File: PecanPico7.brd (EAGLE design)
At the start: 34.2 x 50 mm, 177 parts, among them IC1 Si4464-B1B-FM, IC10 TC1185-1.8VCT713, IC11 TC1185-2.5VCT713, IC12 ADR380ARTZ, IC13 RF6886, IC15 MPU-9250, IC16 PAC1720-1-AIA-TR, IC2 Si4464-B1B-FM, IC3 BME280_BME280, IC4 UBLOX_MAX-6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

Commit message: Fixed incorrect voltage supply at OV2640
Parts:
- removed C55: 470pF, PecanPico6:0402
- removed C56, C57: 1uF, PecanPico6:0402
- removed C58: 100nF, PecanPico6:0402
- removed IC11: TC1185-2.5VCT713, stm32f42x:SOT95P290X145-5N
- removed IC12: ADR380ARTZ, stm32f4:SOT95P237X112-3N
- IC10: value TC1185-1.8VCT713 -> LP5951MF-1.3/NOPB
- TCXO: value TXC_7Z -> TG-5006CJ-19H
- moved R39 17.0 mm to (22.7, 12.8), turned to 270 degrees
- moved R40 15.5 mm to (21.6, 12.8), turned to 270 degrees
- moved C34 6.08 mm to (26.4, 18.3), flipped to the top
- moved C40 4.24 mm to (14.6, 10.8), turned to 270 degrees
- moved R22 3.62 mm to (23.0, 11.4), turned to 0 degrees
- moved R25 3.60 mm to (15.0, 8.20), turned to 90 degrees
- moved C54 2.88 mm to (18.2, 8.80), turned to 0 degrees
- moved Q2 2.75 mm to (20.2, 10.4), turned to 90 degrees
- moved R32 2.51 mm to (30.0, 13.7), turned to 90 degrees
- moved IC10 2.14 mm to (16.8, 11.5)
- moved C30 2.02 mm to (21.0, 21.1)
- moved C42 1.75 mm to (16.4, 7.70), turned to 180 degrees
- moved C41 1.49 mm to (16.4, 8.80)
- moved C53 1.39 mm to (19.0, 13.2), turned to 270 degrees
- moved R31 1.20 mm to (28.9, 13.7), turned to 90 degrees
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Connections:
- net CAM_VCC1V8 renamed CAM_VCC1V3
- removed net CAM_VCC3V0: C43.P$1, C53.P$2, C56.P$2, IC10.1, IC10.3, IC11.1, IC11.3, Q2.3, X1.11, X1.6
- removed net N$28: C55.P$2, IC11.4
- removed net N$30: C37.P$1, C39.P$1, IC12.2, IC5.P1
- net CAM_VCC2V5: now also C43.P$1, C53.P$2, IC10.1, IC10.3, Q2.3, R39.P$2, R40.P$2, X1.11, X1.6; no longer C57.P$2, IC11.5
- net GND: no longer C55.P$1, C56.P$1, C57.P$1, C58.P$2, IC11.2, IC12.3
- net VCC: now also C37.P$1, C39.P$1, IC5.P1; no longer C58.P$1, IC12.1, R39.P$2, R40.P$2
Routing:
- net CAM_VCC3V0: track 25.3 -> 0.00 mm
- net CAM_VCC2V5: track 5.85 -> 24.8 mm
- net CAM_SIOC: track 27.4 -> 16.5 mm, vias 3 -> 2
- net CAM_SIOD: track 28.8 -> 18.2 mm, vias 3 -> 2
- net LED2: track 31.6 -> 25.3 mm, vias 3 -> 1
- net AGND: track 8.84 -> 3.30 mm, vias 2 -> 0
- net VCC: track 284.5 -> 279.1 mm, vias 26 -> 25
- net CAM_OFF: track 4.94 -> 10.1 mm
- net N$30: track 4.54 -> 0.00 mm
- net NRST: track 25.1 -> 21.7 mm
- net GND: track 16.1 -> 18.2 mm, vias 168 -> 178
- net N$48: track 0.98 -> 3.02 mm
- net LED1: track 22.5 -> 20.6 mm
- net N$28: track 1.31 -> 0.00 mm
- net SD_MISO: track 14.2 -> 13.3 mm
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
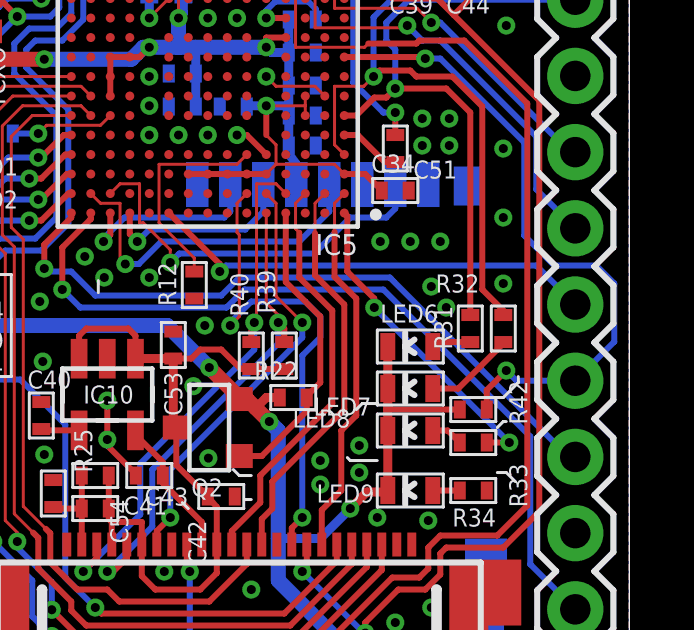
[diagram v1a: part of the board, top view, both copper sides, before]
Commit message: Moved parts around
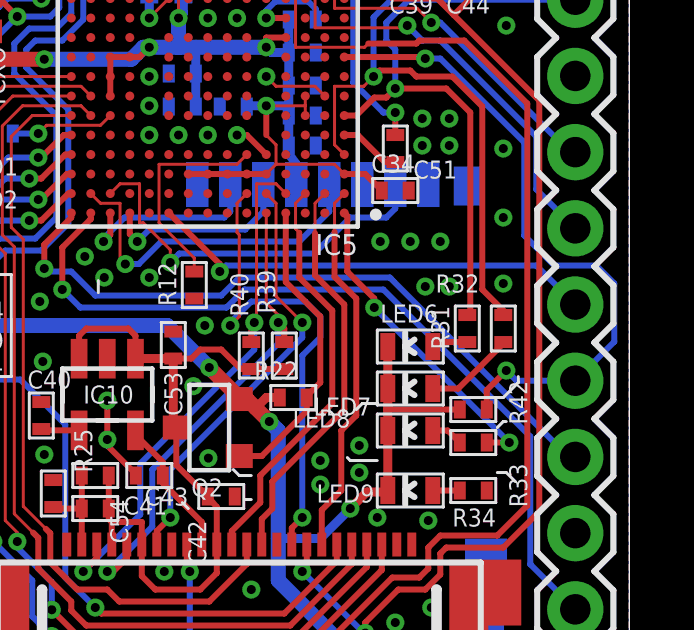
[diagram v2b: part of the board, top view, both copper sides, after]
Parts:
- moved R31 0.10 mm to (28.8, 13.7)
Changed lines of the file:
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@@
 <attribute name="VALUE" x="28" y="9.7" size="0.6" layer="27" rot="R180"/>
 </element>
-<element name="R31" library="PecanPico6" package="0402" value="3.3k" x="28.9" y="13.7" smashed="yes" rot="R90">
-<attribute name="NAME" x="28.3" y="13" size="0.6" layer="25" rot="R90"/>
-<attribute name="VALUE" x="30.1" y="13" size="0.6" layer="27" rot="R90"/>
+<element name="R31" library="PecanPico6" package="0402" value="3.3k" x="28.8" y="13.7" smashed="yes" rot="R90">
+<attribute name="NAME" x="28.2" y="13" size="0.6" layer="25" rot="R90"/>
+<attribute name="VALUE" x="30" y="13" size="0.6" layer="27" rot="R90"/>
 </element>
 <element name="R32" library="PecanPico6" package="0402" value="1k" x="30" y="13.7" smashed="yes" rot="R90">
@@
 <via x="12.63" y="32.5" extent="1-16" drill="0.3"/>
 <via x="27.9" y="16.6" extent="1-16" drill="0.3"/>
-<via x="28.1" y="14.4" extent="1-16" drill="0.3"/>
+<via x="28.2" y="15.1" extent="1-16" drill="0.3"/>
 <via x="16.4" y="49" extent="1-16" drill="0.3"/>
 <via x="24.3" y="42.9" extent="1-16" drill="0.3"/>
@@
 <contactref element="X1" pad="P$3"/>
 <contactref element="X1" pad="P$4"/>
-<via x="27.6" y="15.1" extent="1-16" drill="0.3"/>
+<via x="27.4" y="15.1" extent="1-16" drill="0.3"/>
 <via x="16.8" y="11.3" extent="1-16" drill="0.3"/>
 <wire x1="17.75" y1="8.8" x2="17.75" y2="8.85" width="0.2" layer="1"/>
@@
 <contactref element="LED6" pad="A"/>
 <contactref element="R31" pad="P$1"/>
-<wire x1="28.9" y1="13.25" x2="27.65" y2="13.25" width="0.2" layer="1"/>
+<wire x1="28.8" y1="13.25" x2="27.65" y2="13.25" width="0.2" layer="1"/>
 <wire x1="27.65" y1="13.25" x2="27.65" y2="13.1" width="0.2" layer="1"/>
 </signal>
@@
 <wire x1="26.4" y1="23" x2="26.1" y2="23.3" width="0.2" layer="16"/>
 <wire x1="26.1" y1="23.3" x2="26.1" y2="23.9" width="0.2" layer="16"/>
-<wire x1="28.9" y1="20.9" x2="28.9" y2="14.15" width="0.2" layer="1"/>
 <wire x1="25.1" y1="20.8" x2="25.7" y2="21.4" width="0.2" layer="1"/>
 <wire x1="25.7" y1="21.4" x2="26.1" y2="21.4" width="0.2" layer="1"/>
@@
 <wire x1="26.1" y1="23.9" x2="26.86" y2="24.66" width="0.2" layer="16"/>
 <wire x1="26.86" y1="24.66" x2="32.4" y2="24.66" width="0.2" layer="16"/>
+<wire x1="28.9" y1="20.9" x2="28.9" y2="14.15" width="0.2" layer="1"/>
+<wire x1="28.9" y1="14.15" x2="28.8" y2="14.15" width="0.2" layer="1"/>
 </signal>
 <signal name="LED3">

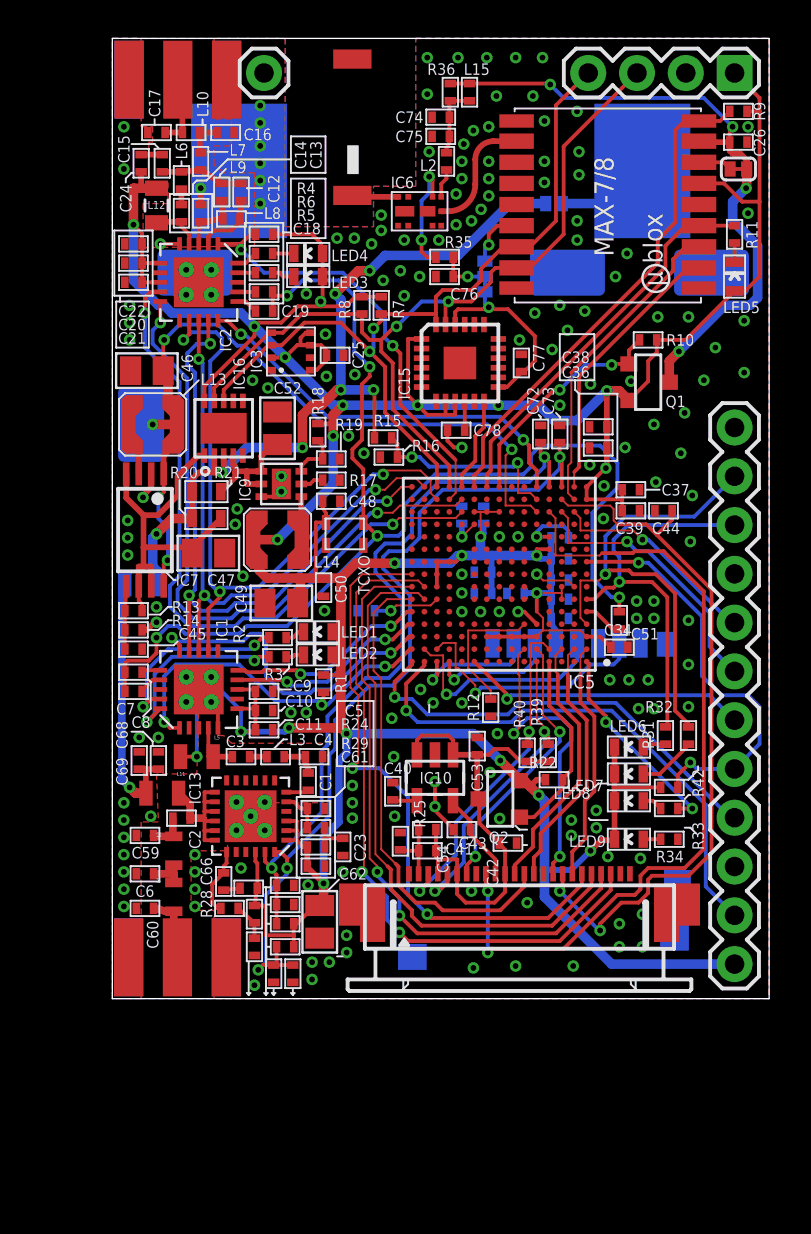
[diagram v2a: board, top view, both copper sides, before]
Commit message: Relocated names, added infos, added PCB name
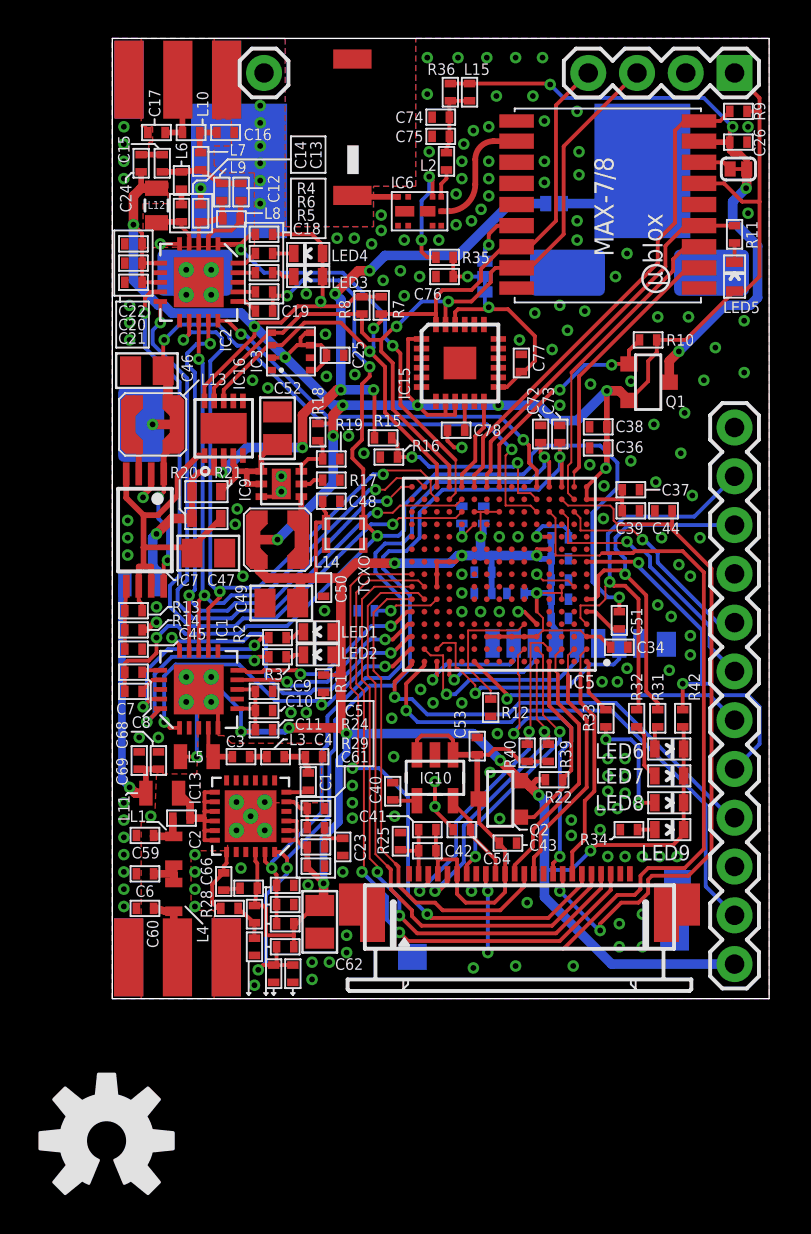
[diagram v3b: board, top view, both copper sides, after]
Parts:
- added LOGO1: OSHW-LOGOL, PecanPico6:OSHW-LOGO-L
- IC10: value LP5951MF-1.3/NOPB -> (none)
- moved R33 5.74 mm to (25.7, 14.6), turned to 90 degrees
- moved R42 3.67 mm to (29.7, 14.6), turned to 270 degrees
- moved R32 2.85 mm to (27.3, 14.6)
- moved LED9 2.16 mm to (29.0, 8.80), turned to 270 degrees
- moved R34 2.16 mm to (26.9, 8.80), turned to 180 degrees
- moved LED8 2.10 mm to (29.0, 10.2), turned to 270 degrees
- moved LED6 2.10 mm to (29.0, 13.0), turned to 270 degrees
- moved LED7 2.10 mm to (29.0, 11.6), turned to 270 degrees
- moved R31 0.98 mm to (28.4, 14.6)
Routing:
- net LED3: track 10.7 -> 2.91 mm, vias 2 -> 0
- net N$49: track 1.07 -> 6.27 mm, vias 0 -> 2
- net LED2: track 25.3 -> 21.6 mm
- net VCC: track 279.1 -> 281.0 mm
- net NRST: track 21.7 -> 20.0 mm
- net LED1: track 20.7 -> 19.6 mm
- net CAM_HREF: track 42.5 -> 43.1 mm
- net GND: vias 178 -> 189
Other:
- board text added: "Dec 2015"
- board text added: "GPSBIAS"
- board text added: "Pecan Pico 7 rev1.0"
- board text removed: "GPS BIAS"

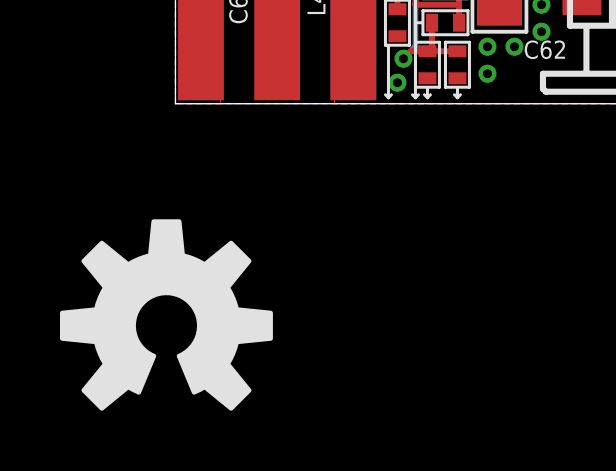
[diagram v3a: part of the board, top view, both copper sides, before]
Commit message: Adjusted symbols
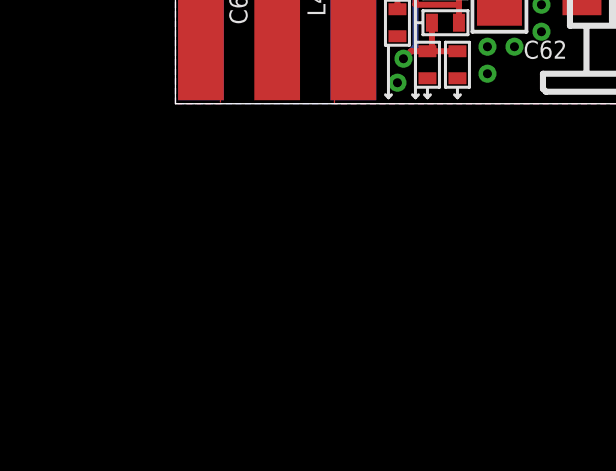
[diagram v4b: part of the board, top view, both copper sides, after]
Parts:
- removed LOGO1: OSHW-LOGOL, PecanPico6:OSHW-LOGO-L
- added LOGO2: OSHW-LOGOM, PecanPico6:OSHW-LOGO-M
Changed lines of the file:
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@@
 <grid distance="0.1" unitdist="mm" unit="mm" style="lines" multiple="1" display="yes" altdistance="0.025" altunitdist="inch" altunit="inch"/>
 <layers>
-<layer number="1" name="Top" color="4" fill="1" visible="yes" active="yes"/>
-<layer number="16" name="Bottom" color="1" fill="1" visible="no" active="yes"/>
+<layer number="1" name="Top" color="4" fill="1" visible="no" active="yes"/>
+<layer number="16" name="Bottom" color="1" fill="1" visible="yes" active="yes"/>
 <layer number="17" name="Pads" color="2" fill="1" visible="yes" active="yes"/>
 <layer number="18" name="Vias" color="2" fill="1" visible="yes" active="yes"/>
 <layer number="19" name="Unrouted" color="6" fill="1" visible="yes" active="yes"/>
 <layer number="20" name="Dimension" color="15" fill="1" visible="yes" active="yes"/>
-<layer number="21" name="tPlace" color="7" fill="1" visible="yes" active="yes"/>
-<layer number="22" name="bPlace" color="7" fill="1" visible="no" active="yes"/>
-<layer number="23" name="tOrigins" color="15" fill="1" visible="yes" active="yes"/>
-<layer number="24" name="bOrigins" color="15" fill="1" visible="no" active="yes"/>
-<layer number="25" name="tNames" color="7" fill="1" visible="yes" active="yes"/>
+<layer number="21" name="tPlace" color="7" fill="1" visible="no" active="yes"/>
+<layer number="22" name="bPlace" color="7" fill="1" visible="yes" active="yes"/>
+<layer number="23" name="tOrigins" color="15" fill="1" visible="no" active="yes"/>
+<layer number="24" name="bOrigins" color="15" fill="1" visible="yes" active="yes"/>
+<layer number="25" name="tNames" color="7" fill="1" visible="no" active="yes"/>
 <layer number="26" name="bNames" color="7" fill="1" visible="yes" active="yes"/>
 <layer number="27" name="tValues" color="7" fill="1" visible="no" active="yes"/>
@@
 <layer number="35" name="tGlue" color="7" fill="4" visible="no" active="yes"/>
 <layer number="36" name="bGlue" color="7" fill="5" visible="no" active="yes"/>
-<layer number="37" name="tTest" color="7" fill="1" visible="yes" active="yes"/>
-<layer number="38" name="bTest" color="7" fill="1" visible="no" active="yes"/>
+<layer number="37" name="tTest" color="7" fill="1" visible="no" active="yes"/>
+<layer number="38" name="bTest" color="7" fill="1" visible="yes" active="yes"/>
 <layer number="39" name="tKeepout" color="4" fill="11" visible="yes" active="yes"/>
 <layer number="40" name="bKeepout" color="1" fill="11" visible="yes" active="yes"/>
@@
 <layer number="49" name="Reference" color="7" fill="1" visible="yes" active="yes"/>
 <layer number="50" name="dxf" color="7" fill="1" visible="yes" active="yes"/>
-<layer number="51" name="tDocu" color="7" fill="1" visible="yes" active="yes"/>
-<layer number="52" name="bDocu" color="7" fill="1" visible="no" active="yes"/>
+<layer number="51" name="tDocu" color="7" fill="1" visible="no" active="yes"/>
+<layer number="52" name="bDocu" color="7" fill="1" visible="yes" active="yes"/>
 <layer number="53" name="tGND_GNDA" color="7" fill="1" visible="yes" active="yes"/>
 <layer number="54" name="bGND_GNDA" color="7" fill="1" visible="yes" active="yes"/>
@@
 <attribute name="OC_NEWARK" value="unknown" x="21.2" y="4" size="0.6" layer="27" display="off"/>
 </element>
-<element name="LOGO1" library="PecanPico6" package="OSHW-LOGO-L" value="OSHW-LOGOL" x="-0.3" y="-7.4"/>
+<element name="LOGO2" library="PecanPico6" package="OSHW-LOGO-M" value="OSHW-LOGOM" x="6.4" y="18.4" rot="MR90"/>
 </elements>
 <signals>
